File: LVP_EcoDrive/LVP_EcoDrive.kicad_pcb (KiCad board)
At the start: 2 copper layers, 196 x 74.5 mm, 49 parts, among them J1 Conn_02x05_Odd_Even, J10 Conn_01x02_Pin, J11 Conn_01x02_Pin, J12 Conn_01x02_Pin, J13 Conn_01x02_Pin, J2 Conn_02x05_Odd_Even, J3 Conn_02x05_Odd_Even, J4 Conn_02x05_Odd_Even, J5 Conn_02x05_Odd_Even, J6 Conn_02x20_Odd_Even, J7 Conn_01x02_Pin, J8 Conn_01x02_Pin, J9 Screw_Terminal_01x11, Q2 AO3400A, U1 SSIT3490EESA, U2 SSIT3490EESA, U3 SSIT3490EESA, U4 AMS1117-5.0, U5 LM311, U6 LM311, U7 LM311

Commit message: LVP_EcoDrive Done, Finalized
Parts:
- removed R19, R20: 330, Resistor_SMD:R_1206_3216Metric_Pad1.30x1.75mm_HandSolder
- added C1: 10u, Capacitor_SMD:C_1206_3216Metric_Pad1.33x1.80mm_HandSolder, F.Cu at (95.1, 90.5)
- added C10: 100uF, Capacitor_SMD:CP_Elec_8x6.5, F.Cu at (75.2, 67.2)
- added C2: 10u, Capacitor_SMD:C_1206_3216Metric_Pad1.33x1.80mm_HandSolder, F.Cu at (95.1, 92.9)
- added C3: 0.1u, Capacitor_SMD:C_1206_3216Metric_Pad1.33x1.80mm_HandSolder, F.Cu at (238.4, 81.0)
- added C4: 0.1u, Capacitor_SMD:C_1206_3216Metric_Pad1.33x1.80mm_HandSolder, F.Cu at (238.4, 75.1)
- added C5: 0.1u, Capacitor_SMD:C_1206_3216Metric_Pad1.33x1.80mm_HandSolder, F.Cu at (238.2, 87.4)
- added C6: 10u, Capacitor_SMD:C_1206_3216Metric_Pad1.33x1.80mm_HandSolder, F.Cu at (68.5, 65.2)
- added C7: 0.1u, Capacitor_SMD:C_1206_3216Metric_Pad1.33x1.80mm_HandSolder, F.Cu at (106.5, 84.4)
- added C8: 47uF, Capacitor_SMD:CP_Elec_5x5.4, F.Cu at (183.7, 65.1)
- added C9: 100uF, Capacitor_SMD:CP_Elec_8x6.5, F.Cu at (207.1, 66.8)
- added D4: SMBJ5.0A_C83333, EasyEDA:SMB_L4.6-W3.6-LS5.3-RD, F.Cu at (175.2, 65.0)
- added D5: SMBJ12A_C151251, EasyEDA:SMB_L4.6-W3.6-LS5.3-RD, F.Cu at (214.5, 66.4)
- added J14: Conn_02x05_Odd_Even, Connector_IDC:IDC-Header_2x05_P2.54mm_Vertical, F.Cu at (208.3, 98.9)
- added J15: Conn_01x05_Pin, Connector_PinHeader_1.27mm:PinHeader_1x05_P1.27mm_Vertical_SMD_Pin1Right, F.Cu at (225.5, 81.9)
- D1, D3: footprint LED_SMD:LED_1206_3216Metric_Pad1.42x1.75mm_HandSolder -> LED_SMD:LED_0603_1608Metric
- R1, R2, R3, R4, R5, R6: value 100 -> 220; footprint Resistor_SMD:R_1206_3216Metric_Pad1.30x1.75mm_HandSolder -> Resistor_SMD:R_0603_1608Metric_Pad0.98x0.95mm_HandSolder; moved to B.Cu
- R10, R12, R14, R15, R8, R9: moved to B.Cu
- R16, R7: footprint Resistor_SMD:R_1206_3216Metric_Pad1.30x1.75mm_HandSolder -> Resistor_SMD:R_0603_1608Metric_Pad0.98x0.95mm_HandSolder
- moved R16 154.1 mm to (219.5, 63.9), turned to 90 degrees
- moved D3 153.9 mm to (219.5, 67.2), turned to -90 degrees
- moved R7 152.3 mm to (217.9, 63.9), turned to 90 degrees
- moved D1 152.2 mm to (217.9, 67.2), turned to -90 degrees
- moved R2 64.9 mm to (167.7, 96.4), turned to 90 degrees
- moved R1 63.4 mm to (167.7, 88.6), turned to 90 degrees
- moved R21 40.5 mm to (86.3, 87.6), turned to 180 degrees
- moved R13 40.5 mm to (70.0, 100.4), turned to -90 degrees
- moved U5 40.0 mm to (89.6, 82.1)
- moved R5 36.8 mm to (165.2, 96.5), turned to 90 degrees
- moved R11 36.1 mm to (69.9, 95.3)
- moved D2 35.0 mm to (66.3, 69.4), turned to 180 degrees
- moved R3 34.1 mm to (165.1, 88.5), turned to 90 degrees
- moved Q2 34.0 mm to (66.1, 94.7), turned to 180 degrees
- moved R17 28.5 mm to (84.7, 83.6)
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- renumbered J5 to J1, J4 to J2, J2 to J4, J1 to J5
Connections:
- J1 pad 10: unconnected-(J5-Pin_10-Pad10) -> /Csense_{A}
- J1 pad 3: /HVDC_Cnd -> /HIN_{A}
- J1 pad 4: /CBUS_Cnd -> /LIN_{A}
- J1 pad 5: /BRAKE -> unconnected-(J1-Pin_5-Pad5)
- J1 pad 6: /PRECHARGE0 -> unconnected-(J1-Pin_6-Pad6)
- J1 pad 7: /PRECHARGE1 -> unconnected-(J1-Pin_7-Pad7)
- J1 pad 9: unconnected-(J5-Pin_9-Pad9) -> /Phase_Cnd_{A}
- J2 pad 10: unconnected-(J4-Pin_10-Pad10) -> /Csense_{B}
- J2 pad 3: +12V -> /HIN_{B}
- J2 pad 4: GND -> /LIN_{B}
- J2 pad 5: +5V -> unconnected-(J2-Pin_5-Pad5)
- J2 pad 6: GND -> unconnected-(J2-Pin_6-Pad6)
- J2 pad 7: /-12V -> unconnected-(J2-Pin_7-Pad7)
- J2 pad 8: GND -> unconnected-(J2-Pin_8-Pad8)
- J2 pad 9: unconnected-(J4-Pin_9-Pad9) -> /Phase_Cnd_{B}
- J4 pad 10: /Csense_{B} -> unconnected-(J4-Pin_10-Pad10)
- J4 pad 3: /HIN_{B} -> +12V
- J4 pad 4: /LIN_{B} -> GND
- J4 pad 5: unconnected-(J2-Pin_5-Pad5) -> +5V
- J4 pad 6: unconnected-(J2-Pin_6-Pad6) -> GND
- J4 pad 7: unconnected-(J2-Pin_7-Pad7) -> /-12V
- J4 pad 8: unconnected-(J2-Pin_8-Pad8) -> GND
- J4 pad 9: /Phase_Cnd_{B} -> unconnected-(J4-Pin_9-Pad9)
- J5 pad 10: /Csense_{A} -> unconnected-(J5-Pin_10-Pad10)
- J5 pad 3: /HIN_{A} -> /HVDC_Cnd
- J5 pad 4: /LIN_{A} -> /CBUS_Cnd
- J5 pad 5: unconnected-(J1-Pin_5-Pad5) -> /BRAKE
- J5 pad 6: unconnected-(J1-Pin_6-Pad6) -> /PRECHARGE0
- J5 pad 7: unconnected-(J1-Pin_7-Pad7) -> /PRECHARGE1
- J5 pad 9: /Phase_Cnd_{A} -> unconnected-(J5-Pin_9-Pad9)
- J6 pad 11: /ENC_R3 -> /ENC_R2
- J6 pad 12: /FAN0 -> /ENC_R3
- J6 pad 24: GND -> /FAN0
- J6 pad 7: /ENC_R1 -> /EXP_INT
- J6 pad 8: /ENC_T1 -> /ENC_R1
- J6 pad 9: /ENC_R2 -> /ENC_T1
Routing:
- net /LIN_{A}: track 0.01 -> 109.2 mm, vias 0 -> 2
- net /PRECHARGE0: track 0.00 -> 103.7 mm, vias 0 -> 2
- net /BRAKE: track 0.00 -> 97.8 mm, vias 0 -> 2
- net /PRECHARGE1: track 0.00 -> 96.8 mm, vias 0 -> 2
- net /HIN_{A}: track 1.39 -> 93.8 mm, vias 0 -> 2
- net /FAN0: track 0.00 -> 91.6 mm, vias 0 -> 1
- net /~{BKIN}: track 22.5 -> 109.9 mm, vias 0 -> 3
- net /ENC_R3: track 0.00 -> 84.9 mm, vias 0 -> 1
- net /ENC_R2: track 0.00 -> 83.6 mm, vias 0 -> 1
- net /ENC_R1: track 0.00 -> 81.9 mm, vias 0 -> 1
- net /ENC_T1: track 0.00 -> 81.5 mm, vias 0 -> 1
- net /TEMP1: track 0.00 -> 80.0 mm, vias 0 -> 3
- net /Csense_{C}: track 16.9 -> 91.0 mm, vias 0 -> 4
- net /TEMP2: track 0.00 -> 73.1 mm, vias 0 -> 3
- net /LIN_{B}: track 0.01 -> 72.2 mm, vias 0 -> 2
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- added copper zone on B.Cu, net +5V
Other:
- board size 196 x 74.5 mm -> 196 x 44.2 mm

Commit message: Added : Fused Inputs for LVP
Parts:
- added F1: Fuse_Small, Fuse:Fuse_2512_6332Metric, F.Cu at (207.3, 66.0)
- added F2: Fuse_Small, Fuse:Fuse_2512_6332Metric, F.Cu at (183.5, 65.9)
- moved D4 71.2 mm to (246.4, 65.7), turned to 90 degrees
- moved D3 30.0 mm to (249.5, 67.3)
- moved R16 30.0 mm to (249.5, 64.0)
- moved D5 25.5 mm to (240.0, 65.7)
- moved D1 25.2 mm to (243.1, 67.3)
- moved R7 25.2 mm to (243.1, 64.1)
- moved C9 10.0 mm to (217.1, 66.4), turned to 0 degrees
- moved C8 8.43 mm to (175.3, 65.8), turned to 180 degrees
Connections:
- J4 pad 1: +12V -> Net-(J4-Pin_1)
- J4 pad 3: +12V -> Net-(J4-Pin_1)
- J4 pad 5: +5V -> Net-(J4-Pin_5)
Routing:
- net Net-(J4-Pin_5): track 0.00 -> 13.9 mm, vias 0 -> 4
- net Net-(J4-Pin_1): track 0.00 -> 7.29 mm
- net +5V: track 275.1 -> 278.8 mm, vias 18 -> 19
- net +12V: track 265.8 -> 268.6 mm
- net GND: vias 316 -> 318
- added copper zone on F.Cu, net +12V

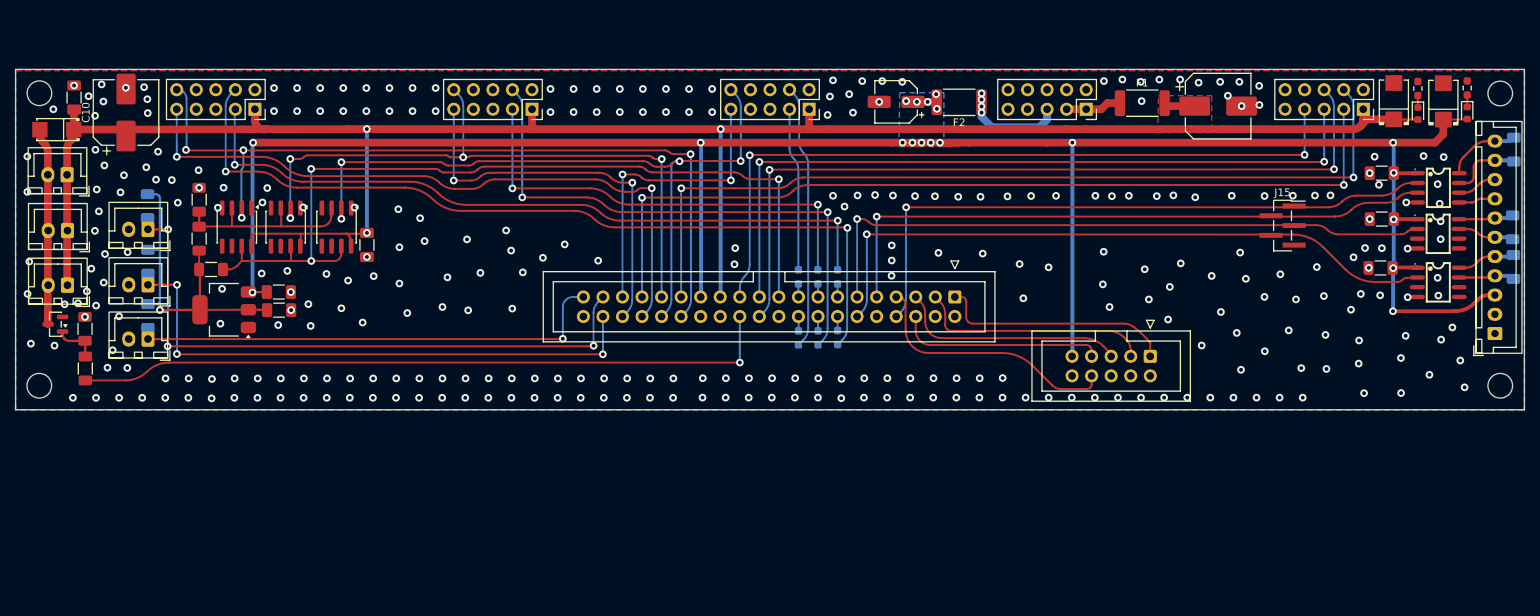
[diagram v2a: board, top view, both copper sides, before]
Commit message: (LVP_Ecodrive) Added : Increase Pcb size by 3-4mm , much better grounding
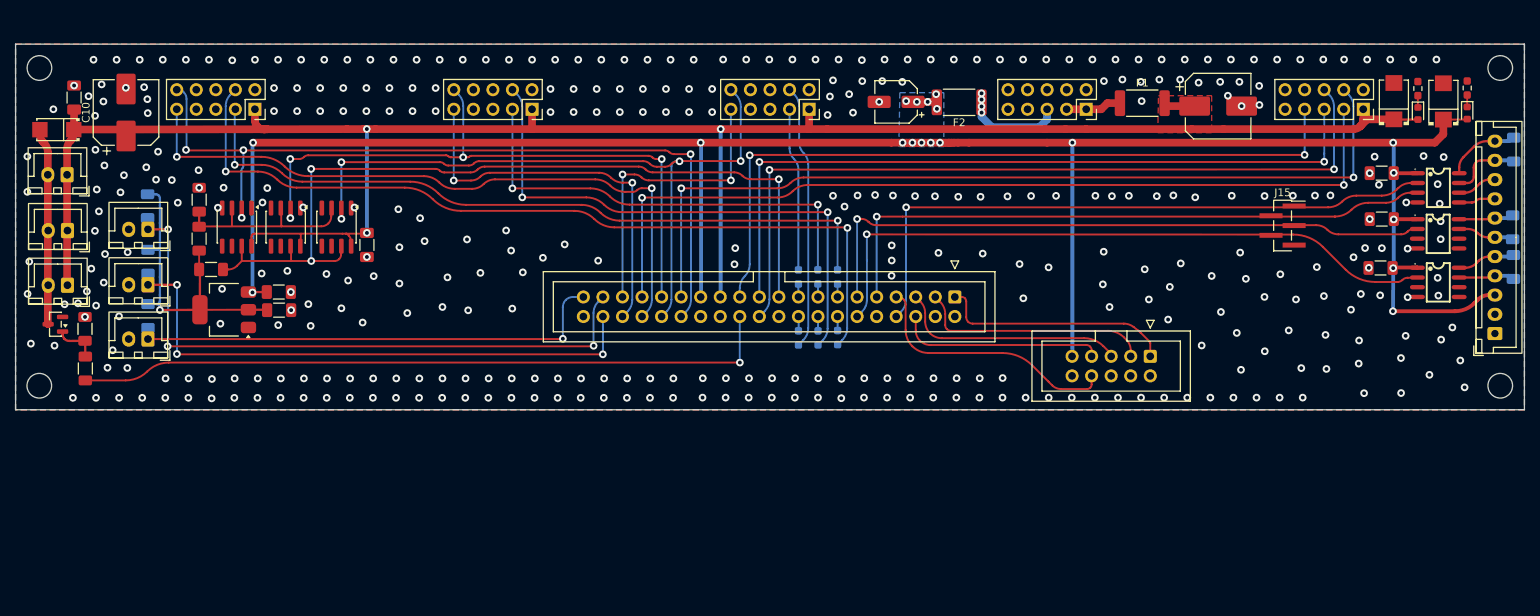
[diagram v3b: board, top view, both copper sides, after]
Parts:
- moved H2 3.31 mm to (253.8, 61.4)
- moved H1 3.28 mm to (64.0, 61.4)
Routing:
- net GND: vias 318 -> 377
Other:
- board size 196 x 44.2 mm -> 196 x 47.5 mm
